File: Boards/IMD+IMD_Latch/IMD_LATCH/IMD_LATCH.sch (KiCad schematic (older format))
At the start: 29 parts, among them J1 UF_5_VT, J2 MM_F_RA_04, J3 MicroFit_V_2, K1 G5Q-1A4-DC5-5V, Q1 SSM3K333R, Q2 SSM3K333R, U1 TLV3701QDBVRG4Q1, U2 CD4043BPWR, U3 TLV3701QDBVRG4Q1

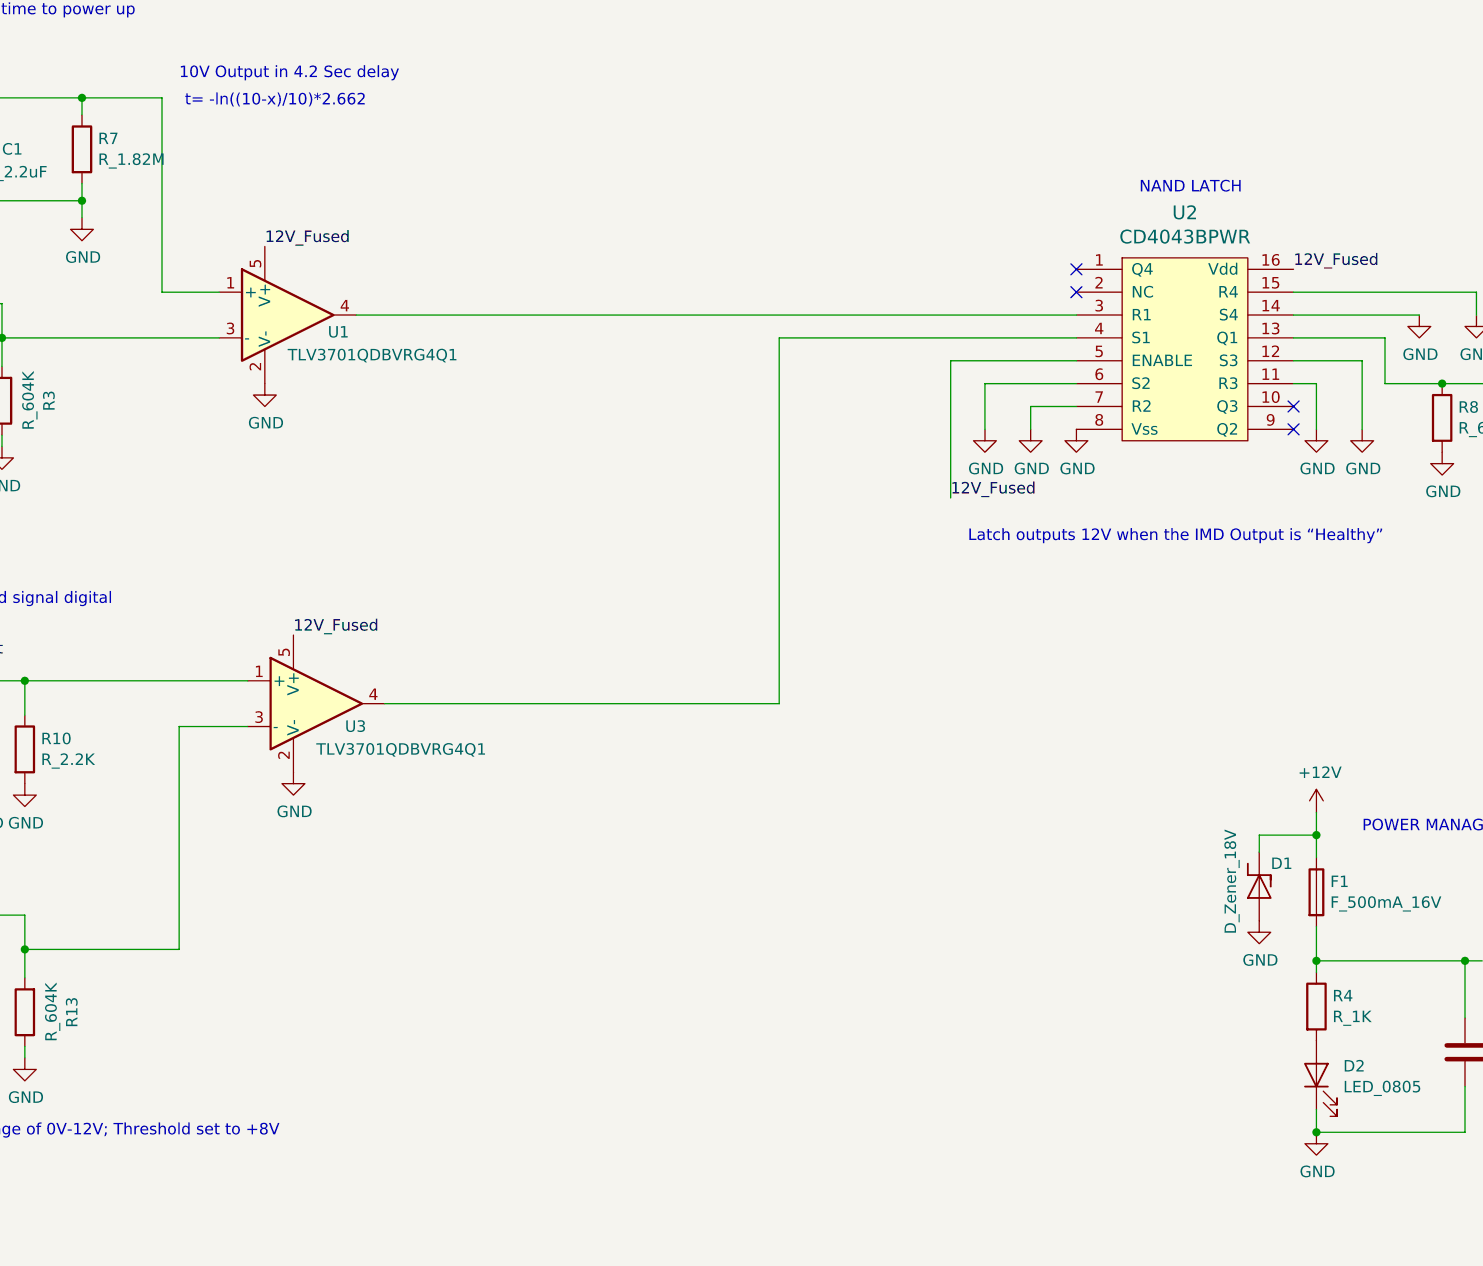
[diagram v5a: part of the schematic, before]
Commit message: Fixed IMD Latch Schematic + Finished Layout
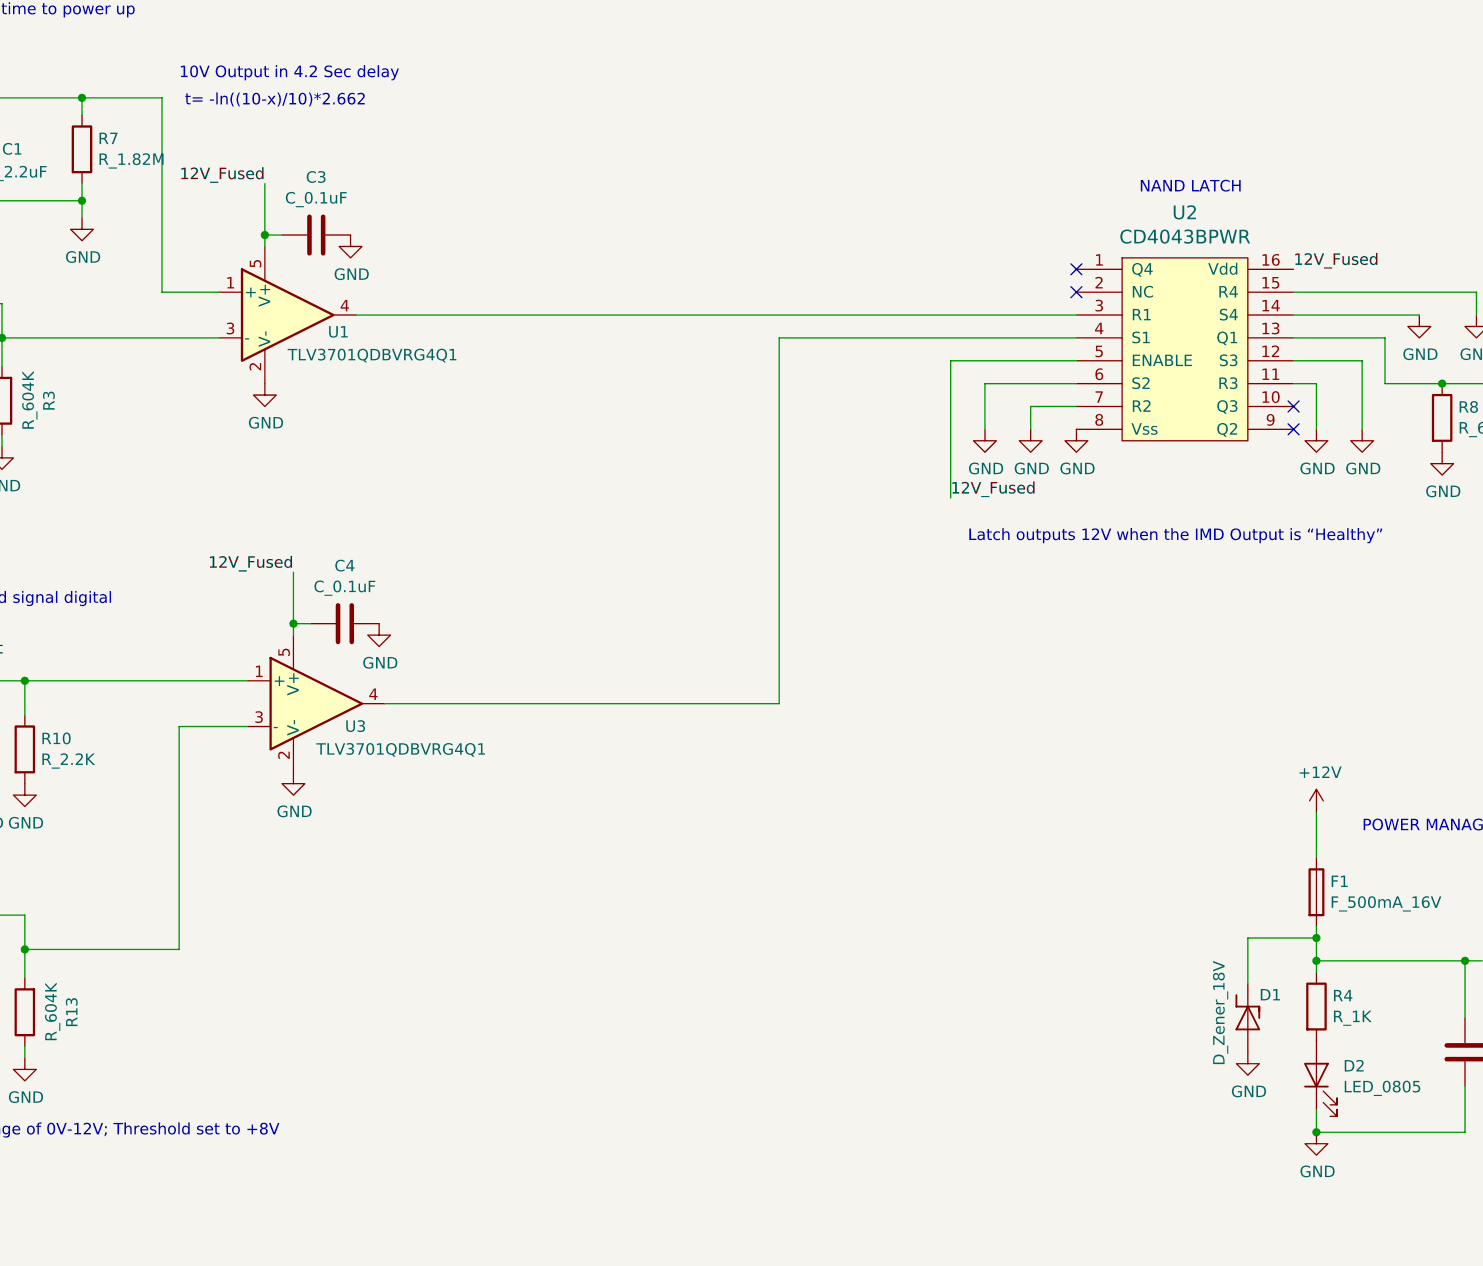
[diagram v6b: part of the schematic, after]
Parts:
- added C3, C4: C_0.1uF, footprints:C_0805_OEM, symbol footprints:C_0.1uF
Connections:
- net +12V: no longer D1.1 (K)
- net 12V_Fused: now also D1.1 (K), C3.2, C4.2
- net GND: now also C3.1, C4.1
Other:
- moved on the sheet: D1
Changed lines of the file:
@@
 L IMD_LATCH-rescue:D_Zener_18V-Formula D1
 U 1 1 5DEA1387
-P 7550 5100
-F 0 "D1" V 7450 5150 50  0000 L CNN
-F 1 "D_Zener_18V" H 7300 4975 50  0000 L CNN
-F 2 "footprints:DO-214AA" H 7450 5100 50  0001 C CNN
-F 3 "http://www.mccsemi.com/up_pdf/SMBJ5338B-SMBJ5388B(SMB).pdf" H 7550 5200 50  0001 C CNN
-F 4 "DK" H 7750 5400 60  0001 C CNN "MFN"
-F 5 "SMBJ5355B-TPMSCT-ND" H 7650 5300 60  0001 C CNN "MPN"
-F 6 "https://www.digikey.com/products/en?keywords=SMBJ5355B-TPMSCT-ND" H 7950 5600 60  0001 C CNN "PurchasingLink"
-	1    7550 5100
+P 7500 5675
+F 0 "D1" V 7400 5725 50  0000 L CNN
+F 1 "D_Zener_18V" H 7250 5550 50  0000 L CNN
+F 2 "footprints:DO-214AA" H 7400 5675 50  0001 C CNN
+F 3 "http://www.mccsemi.com/up_pdf/SMBJ5338B-SMBJ5388B(SMB).pdf" H 7500 5775 50  0001 C CNN
+F 4 "DK" H 7700 5975 60  0001 C CNN "MFN"
+F 5 "SMBJ5355B-TPMSCT-ND" H 7600 5875 60  0001 C CNN "MPN"
+F 6 "https://www.digikey.com/products/en?keywords=SMBJ5355B-TPMSCT-ND" H 7900 6175 60  0001 C CNN "PurchasingLink"
+	1    7500 5675
 	0    1    1    0
 $EndComp
 Wire Wire Line
-	7550 4875 7800 4875
-Wire Wire Line
-	7800 4875 7800 4775
-Wire Wire Line
-	7800 4875 7800 4975
-Connection ~ 7800 4875
-Wire Wire Line
-	7800 5275 7800 5425
+	7800 5275 7800 5325
 Wire Wire Line
 	7800 5425 8450 5425
@@
 L power:GND #PWR02
 U 1 1 5DEA4CE3
-P 7550 5250
-F 0 "#PWR02" H 7550 5000 50  0001 C CNN
-F 1 "GND" H 7555 5077 50  0000 C CNN
-F 2 "" H 7550 5250 50  0001 C CNN
-F 3 "" H 7550 5250 50  0001 C CNN
-	1    7550 5250
+P 7500 5825
+F 0 "#PWR02" H 7500 5575 50  0001 C CNN
+F 1 "GND" H 7505 5652 50  0000 C CNN
+F 2 "" H 7500 5825 50  0001 C CNN
+F 3 "" H 7500 5825 50  0001 C CNN
+	1    7500 5825
 	1    0    0    -1
 $EndComp
@@
 Text Label 1300 1650 2    50   ~ 0
 12V_Fused
-Text Label 3200 2300 0    50   ~ 0
+Text Label 3200 2025 2    50   ~ 0
 12V_Fused
 $Comp
@@
 	2825 4400 2825 5375
 Wire Wire Line
-	7550 4875 7550 4950
-Wire Wire Line
 	8450 5425 8525 5425
 Connection ~ 8450 5425
-Text Label 3325 4000 0    50   ~ 0
-12V_Fused
 $Comp
 L power:GND #PWR0103
@@
 POWER MANAGEMENT / FUSING\n\n
 $Comp
-L power:+12V #PWR?
+L power:+12V #PWR0104
 U 1 1 5E23166B
 P 6400 7100
-F 0 "#PWR?" H 6400 6950 50  0001 C CNN
+F 0 "#PWR0104" H 6400 6950 50  0001 C CNN
 F 1 "+12V" H 6415 7273 50  0000 C CNN
 F 2 "" H 6400 7100 50  0001 C CNN
@@
 $EndComp
 $Comp
-L power:GND #PWR?
+L power:GND #PWR0105
 U 1 1 5E232244
 P 6050 7100
-F 0 "#PWR?" H 6050 6850 50  0001 C CNN
+F 0 "#PWR0105" H 6050 6850 50  0001 C CNN
 F 1 "GND" H 6055 6927 50  0000 C CNN
 F 2 "" H 6050 7100 50  0001 C CNN
@@
 $EndComp
 $Comp
-L power:PWR_FLAG #FLG?
+L power:PWR_FLAG #FLG0101
 U 1 1 5E23331B
 P 6050 7100
-F 0 "#FLG?" H 6050 7175 50  0001 C CNN
+F 0 "#FLG0101" H 6050 7175 50  0001 C CNN
 F 1 "PWR_FLAG" H 6050 7273 50  0000 C CNN
 F 2 "" H 6050 7100 50  0001 C CNN
@@
 $EndComp
 $Comp
-L power:PWR_FLAG #FLG?
+L power:PWR_FLAG #FLG0102
 U 1 1 5E233B51
 P 6400 7100
-F 0 "#FLG?" H 6400 7175 50  0001 C CNN
+F 0 "#FLG0102" H 6400 7175 50  0001 C CNN
 F 1 "PWR_FLAG" H 6400 7273 50  0000 C CNN
 F 2 "" H 6400 7100 50  0001 C CNN
@@
 	-1   0    0    1
 $EndComp
+$Comp
+L footprints:C_0.1uF C3
+U 1 1 5E24B59E
+P 3425 2250
+F 0 "C3" V 3173 2250 50  0000 C CNN
+F 1 "C_0.1uF" V 3264 2250 50  0000 C CNN
+F 2 "footprints:C_0805_OEM" H 3463 2100 50  0001 C CNN
+F 3 "http://datasheets.avx.com/X7RDielectric.pdf" H 3450 2350 50  0001 C CNN
+F 4 "DK" H 3425 2250 60  0001 C CNN "MFN"
+F 5 "478-3352-1-ND" H 3425 2250 60  0001 C CNN "MPN"
+F 6 "https://www.digikey.com/products/en?keywords=478-3352-1-ND" H 3850 2750 60  0001 C CNN "PurchasingLink"
+	1    3425 2250
+	0    1    1    0
+$EndComp
+Wire Wire Line
+	3200 2025 3200 2250
+Wire Wire Line
+	3275 2250 3200 2250
+Connection ~ 3200 2250
+Wire Wire Line
+	3200 2250 3200 2300
+$Comp
+L power:GND #PWR0106
+U 1 1 5E256312
+P 3575 2250
+F 0 "#PWR0106" H 3575 2000 50  0001 C CNN
+F 1 "GND" H 3580 2077 50  0000 C CNN
+F 2 "" H 3575 2250 50  0001 C CNN
+F 3 "" H 3575 2250 50  0001 C CNN
+	1    3575 2250
+	1    0    0    -1
+$EndComp
+Text Label 3325 3725 2    50   ~ 0
+12V_Fused
+$Comp
+L footprints:C_0.1uF C4
+U 1 1 5E259A2A
+P 3550 3950
+F 0 "C4" V 3298 3950 50  0000 C CNN
+F 1 "C_0.1uF" V 3389 3950 50  0000 C CNN
+F 2 "footprints:C_0805_OEM" H 3588 3800 50  0001 C CNN
+F 3 "http://datasheets.avx.com/X7RDielectric.pdf" H 3575 4050 50  0001 C CNN
+F 4 "DK" H 3550 3950 60  0001 C CNN "MFN"
+F 5 "478-3352-1-ND" H 3550 3950 60  0001 C CNN "MPN"
+F 6 "https://www.digikey.com/products/en?keywords=478-3352-1-ND" H 3975 4450 60  0001 C CNN "PurchasingLink"
+	1    3550 3950
+	0    1    1    0
+$EndComp
+Wire Wire Line
+	3325 3725 3325 3950
+Wire Wire Line
+	3400 3950 3325 3950
+Connection ~ 3325 3950
+Wire Wire Line
+	3325 3950 3325 4000
+$Comp
+L power:GND #PWR0107
+U 1 1 5E259A34
+P 3700 3950
+F 0 "#PWR0107" H 3700 3700 50  0001 C CNN
+F 1 "GND" H 3705 3777 50  0000 C CNN
+F 2 "" H 3700 3950 50  0001 C CNN
+F 3 "" H 3700 3950 50  0001 C CNN
+	1    3700 3950
+	1    0    0    -1
+$EndComp
+Wire Wire Line
+	7800 4775 7800 4975
+Wire Wire Line
+	7500 5525 7500 5325
+Wire Wire Line
+	7500 5325 7800 5325
+Connection ~ 7800 5325
+Wire Wire Line
+	7800 5325 7800 5425
 $EndSCHEMATC

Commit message: IMD Latch Fix Rev 2
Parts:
- removed U1: TLV3701QDBVRG4Q1, footprints:SOT-23-5_OEM, symbol IMD_LATCH-rescue:TLV3701QDBVRG4Q1-Formula
- removed U3: TLV3701QDBVRG4Q1, footprints:SOT-23-5_OEM, symbol formula:TLV3701QDBVRG4Q1
- added U1, U3: TLV3701QDBVRG4Q1, footprints:SOT-23-5_OEM, symbol Formula:TLV3701QDBVRG4Q1
- C1: symbol formula:C_2.2uF -> IMD_LATCH-rescue:C_2.2uF-formula
- C3, C4: symbol footprints:C_0.1uF -> IMD_LATCH-rescue:C_0.1uF-footprints
- J1: symbol formula:UF_5_VT -> IMD_LATCH-rescue:UF_5_VT-formula
- R10: symbol formula:R_2.2K -> IMD_LATCH-rescue:R_2.2K-formula
- R7: symbol formula:R_1.82M -> IMD_LATCH-rescue:R_1.82M-formula
- U2: symbol formula:CD4043BPWR -> IMD_LATCH-rescue:CD4043BPWR-formula
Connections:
- net 12V_Fused: now also U1.5 (V+), U3.5 (V+)
- net GND: now also U1.2 (V-), U3.2 (V-)
- net IMD_Output: now also U3.4 (+)
- net at R6.1, R7.1: now also U1.3 (-); no longer C1.1
- net at R2.1, R3.2: now also C1.1, U1.4 (+)
- net at U2.3 (R1): now also U1.1
- net at R12.1, R13.2: now also U3.3 (-)
- net at U2.4 (S1): now also U3.1
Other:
- moved on the sheet: R1, R2, R3, R5, R6, R7
